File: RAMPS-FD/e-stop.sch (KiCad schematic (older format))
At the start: 14 parts, among them P302 ESTOP, U1 74HCT125, U2 74HCT244

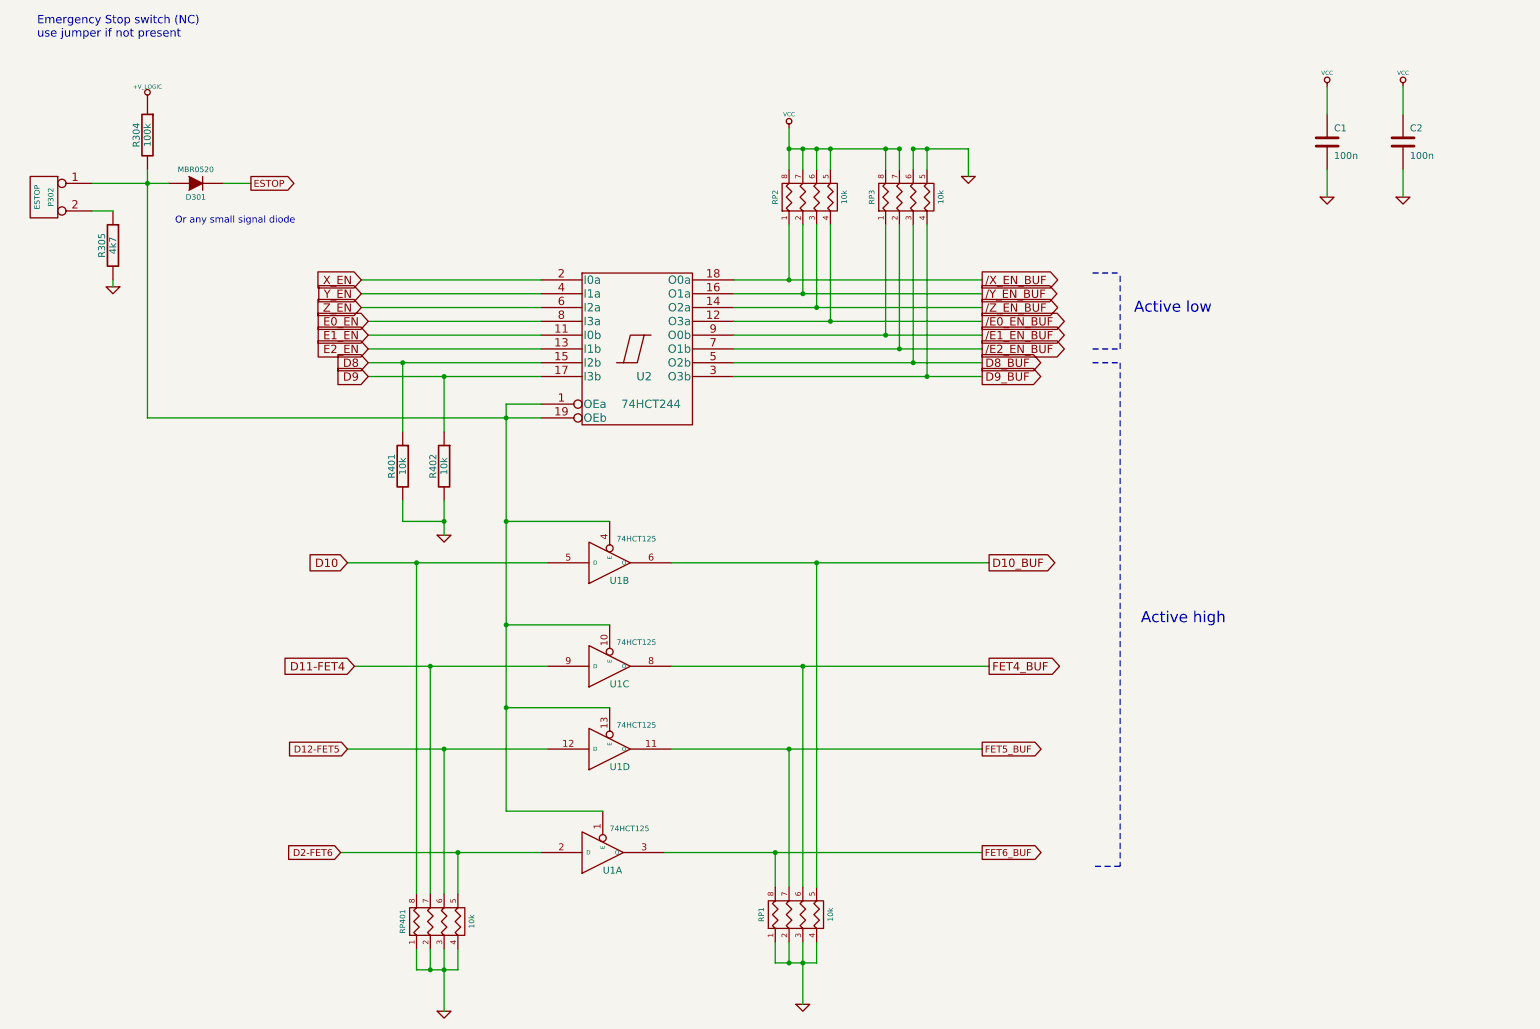
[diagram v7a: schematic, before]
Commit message: RAMPS-FD schematic: remove some redundant pulldowns; add some explanatory notes; update PDF
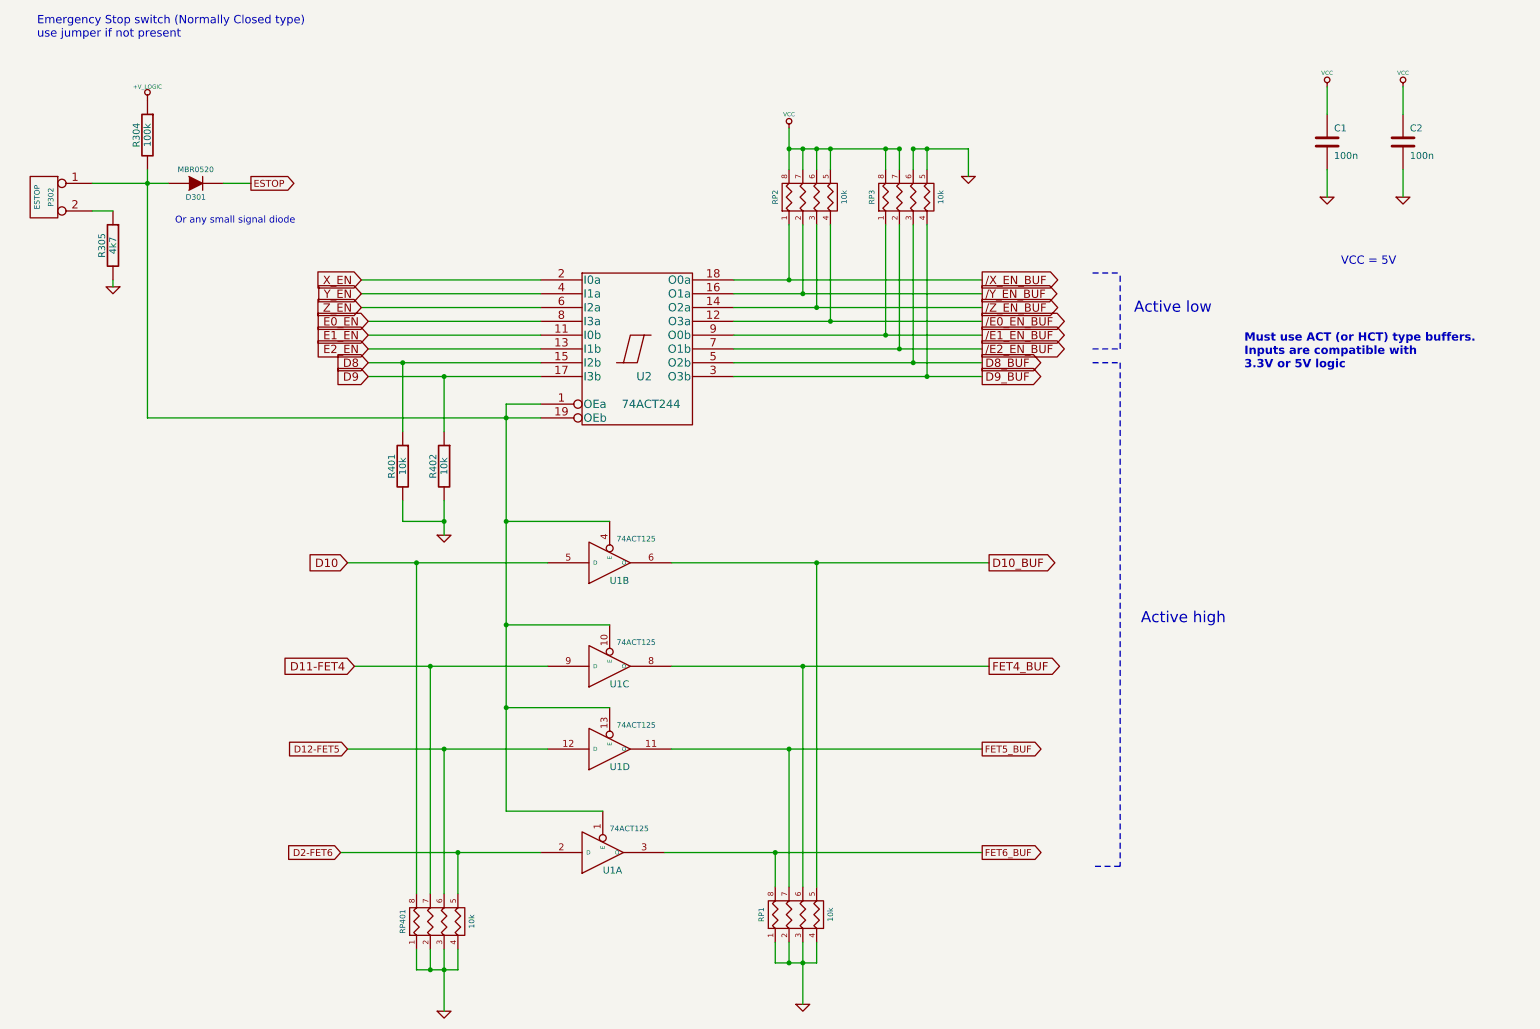
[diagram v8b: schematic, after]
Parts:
- U1: value 74HCT125 -> 74ACT125
- U2: value 74HCT244 -> 74ACT244
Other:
- note added: "Emergency Stop switch (Normally Closed type)\nuse jumper if not present\n\n"
- note added: "Must use ACT (or HCT) type buffers. \nInputs are compatible with \n3.3V or 5V logic"
- note added: "VCC = 5V"
- note removed: "Emergency Stop switch (NC)\nuse jumper if not present\n\n"
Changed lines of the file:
@@
 $EndComp
 Text Notes 750  650  0    60   ~ 0
-Emergency Stop switch (NC)\nuse jumper if not present\n\n
+Emergency Stop switch (Normally Closed type)\nuse jumper if not present\n\n
 Text GLabel 7650 5100 2    60   Output ~ 0
 FET4_BUF
@@
 P 4850 6450
 F 0 "U1" H 4850 6550 50  0000 L BNN
-F 1 "74HCT125" H 4900 6300 40  0000 L TNN
+F 1 "74ACT125" H 4900 6300 40  0000 L TNN
 F 2 "" H 4850 6450 60  0001 C CNN
 F 3 "" H 4850 6450 60  0001 C CNN
@@
 P 4900 5700
 F 0 "U1" H 4900 5800 50  0000 L BNN
-F 1 "74HCT125" H 4950 5550 40  0000 L TNN
+F 1 "74ACT125" H 4950 5550 40  0000 L TNN
 F 2 "" H 4900 5700 60  0001 C CNN
 F 3 "" H 4900 5700 60  0001 C CNN
@@
 P 4900 5100
 F 0 "U1" H 4900 5200 50  0000 L BNN
-F 1 "74HCT125" H 4950 4950 40  0000 L TNN
+F 1 "74ACT125" H 4950 4950 40  0000 L TNN
 F 2 "" H 4900 5100 60  0001 C CNN
 F 3 "" H 4900 5100 60  0001 C CNN
@@
 P 4900 4350
 F 0 "U1" H 4900 4450 50  0000 L BNN
-F 1 "74HCT125" H 4950 4200 40  0000 L TNN
+F 1 "74ACT125" H 4950 4200 40  0000 L TNN
 F 2 "" H 4900 4350 60  0001 C CNN
 F 3 "" H 4900 4350 60  0001 C CNN
@@
 P 5100 2800
 F 0 "U2" H 5150 2600 60  0000 C CNN
-F 1 "74HCT244" H 5200 2400 60  0000 C CNN
+F 1 "74ACT244" H 5200 2400 60  0000 C CNN
 F 2 "" H 5100 2800 60  0001 C CNN
 F 3 "" H 5100 2800 60  0001 C CNN
@@
 	3400 3400 3400 2900
 Connection ~ 3400 2900
+Text Notes 10200 2200 0    60   ~ 0
+VCC = 5V
+Text Notes 9500 2950 0    60   ~ 12
+Must use ACT (or HCT) type buffers. \nInputs are compatible with \n3.3V or 5V logic
 $EndSCHEMATC
